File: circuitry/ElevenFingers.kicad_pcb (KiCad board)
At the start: 2 copper layers, 5.1 x 5.1 mm, 95 parts, among them J1 OLED, SW1 MX, SW10 MX, SW11 MX, SW12 MX, SW13 MX, SW14 MX, SW15 MX, SW16 MX, SW17 MX, SW18 MX, SW19 MX, SW2 MX, SW20 MX, SW21 MX, SW22 MX, SW23 MX, SW24 MX, SW25 MX, SW26 MX, SW27 MX, SW28 MX, SW29 MX, SW3 MX, SW30 MX, SW4 MX, SW5 MX, SW6 MX, SW7 MX, SW8 MX, SW9 MX, U1 ProMicro, U2 TRRS

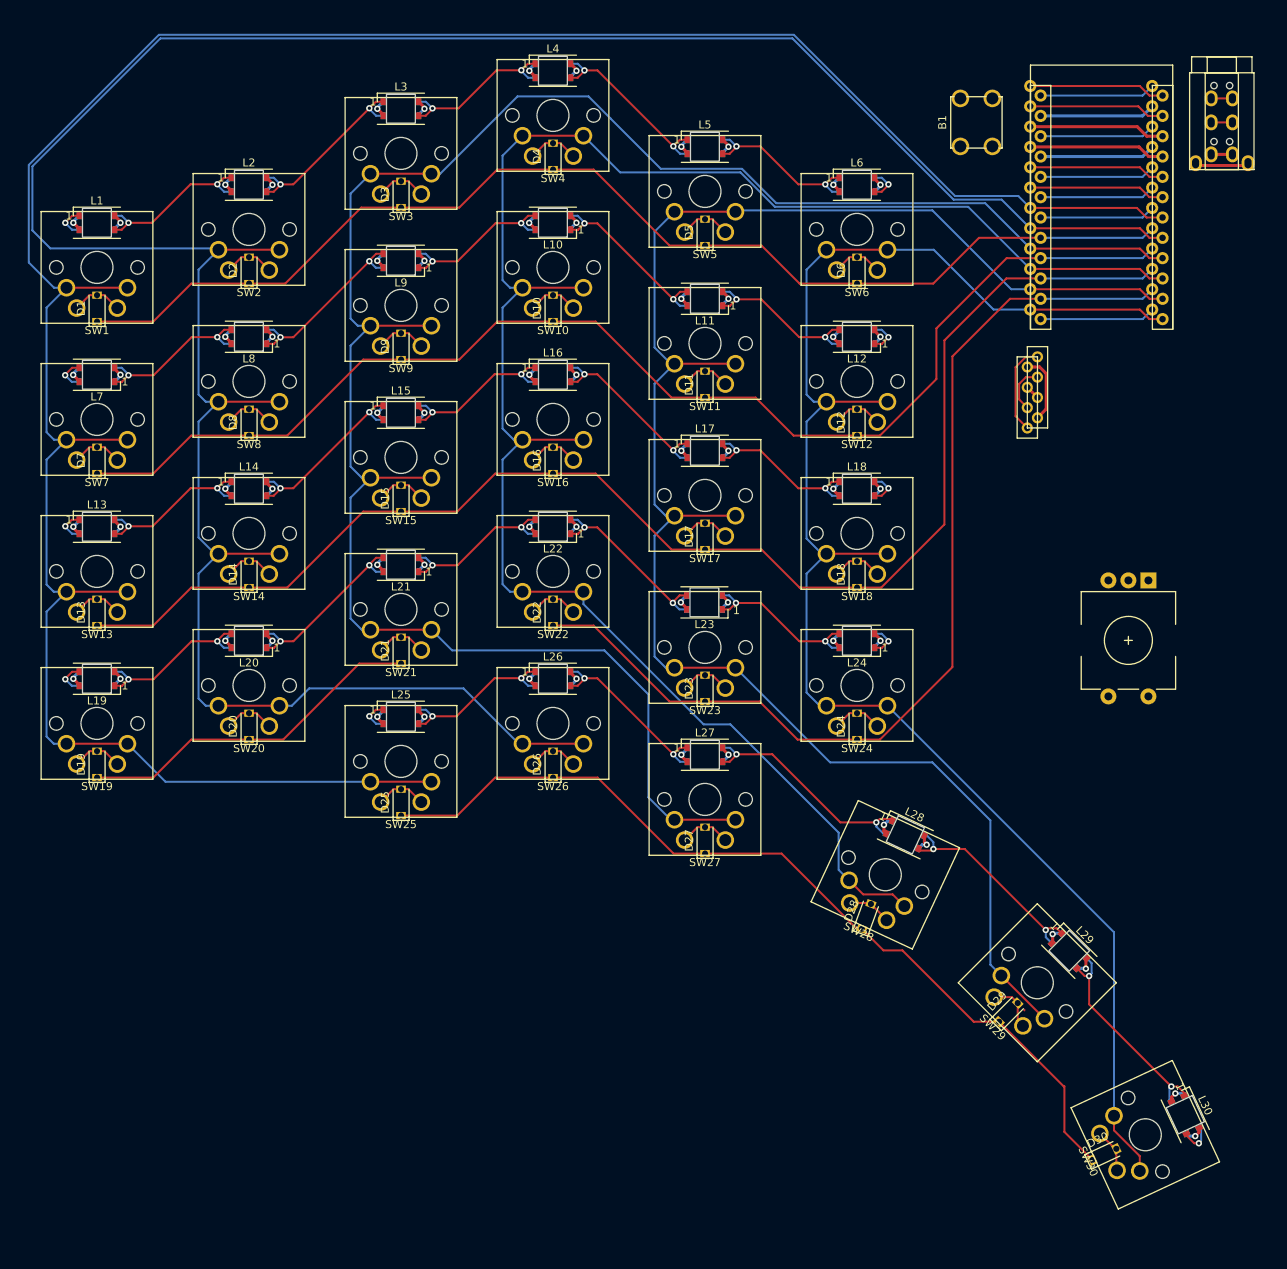
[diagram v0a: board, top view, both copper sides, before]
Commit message: pwr and gnd routed for leds, (not to promicro, and not across rows)
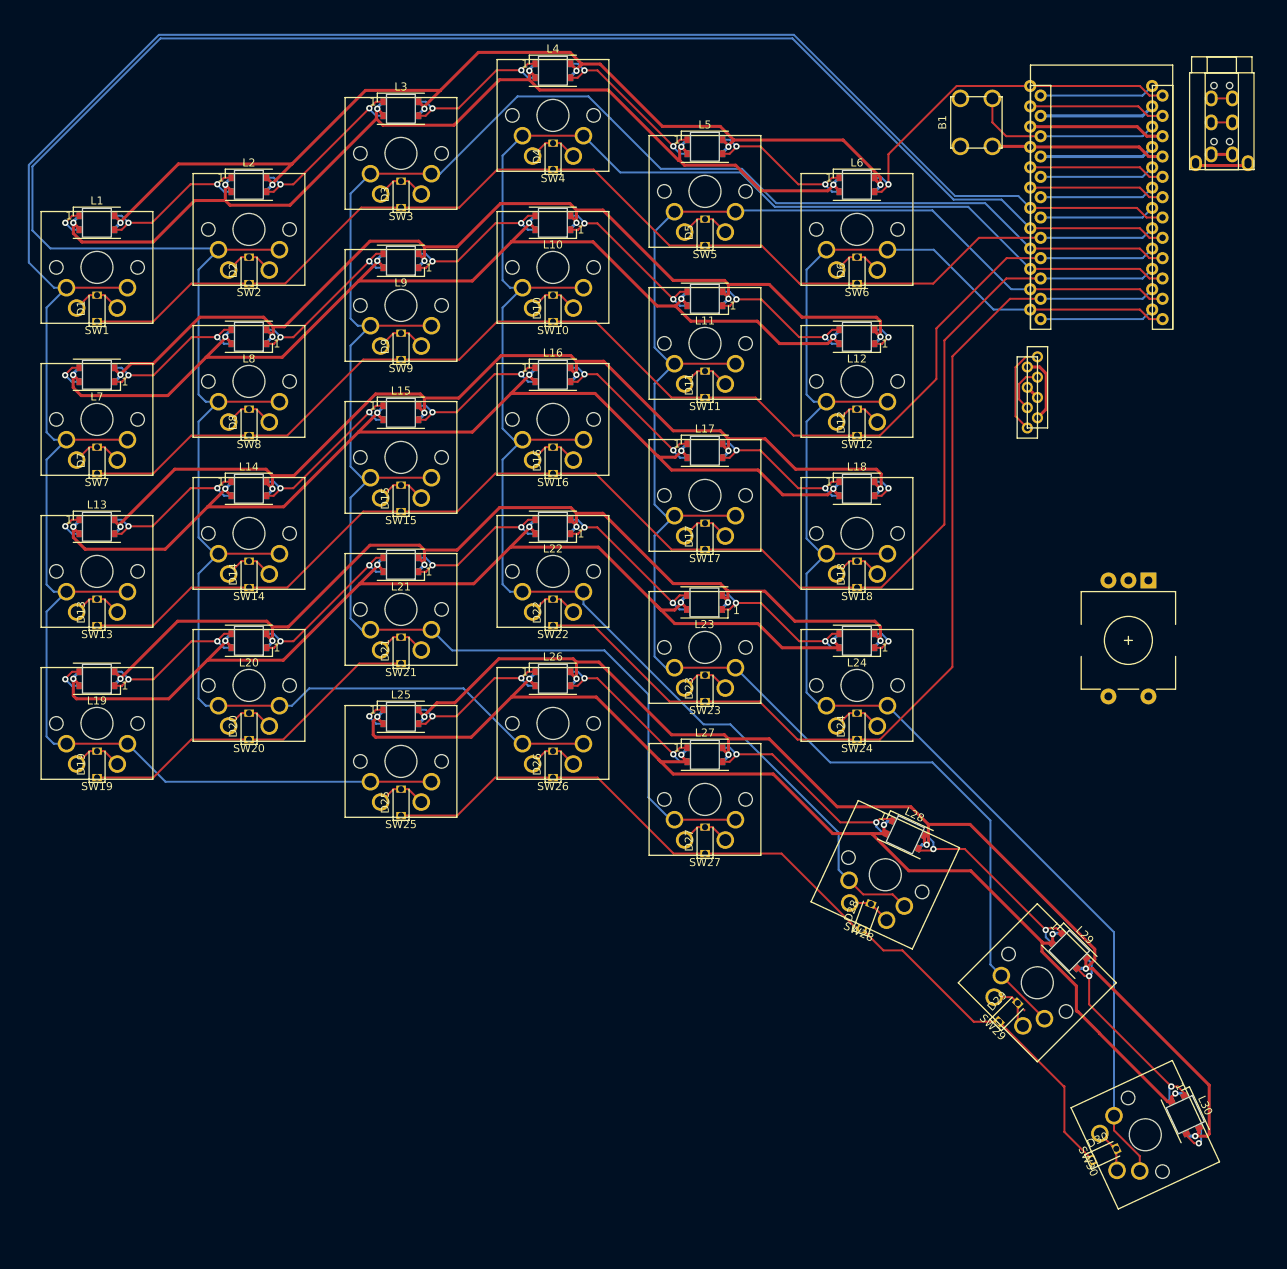
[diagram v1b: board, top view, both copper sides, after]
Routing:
- net GND: track 135.4 -> 767.9 mm
- net VCC: track 89.5 -> 708.5 mm
- net LED: track 21.2 -> 46.3 mm
- net Net-(B1-Pad1): track 14.4 -> 24.2 mm

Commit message: completed tracing?
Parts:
- moved J1 3.66 mm to (158.6, 88.4), turned to 0 degrees
- moved U2 1.29 mm to (176.4, 54.9)
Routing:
- net GND: track 767.9 -> 1000.0 mm
- net VCC: track 708.5 -> 921.5 mm
- net ENC_A: track 14.4 -> 68.4 mm
- net ENC_B: track 14.4 -> 66.5 mm
- net col1: track 328.1 -> 288.1 mm
- net Net-(J1-Pad1): track 28.5 -> 55.5 mm
- net Net-(J1-Pad2): track 23.1 -> 48.9 mm
- net col0: track 312.6 -> 293.8 mm
- net SERIAL: track 19.7 -> 24.8 mm
- net LED: track 46.3 -> 47.4 mm
- net Net-(B1-Pad1): track 24.2 -> 23.3 mm

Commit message: finished tracing and error checking
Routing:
- net row4: track 126.0 -> 267.9 mm
- net Net-(L24-Pad2): track 8.51 -> 109.3 mm
- net Net-(L13-Pad2): track 8.43 -> 29.9 mm
- net Net-(L1-Pad2): track 8.44 -> 29.8 mm
- net row3: track 170.8 -> 191.7 mm
- net Net-(L12-Pad2): track 8.44 -> 28.5 mm
- net col1: track 288.1 -> 276.6 mm
- net col0: track 293.8 -> 284.8 mm
- net GND: track 1000.0 -> 998.4 mm
- net col5: track 204.7 -> 203.2 mm
- net Net-(D29-Pad2): track 6.45 -> 5.45 mm
- net ENC_A: track 68.4 -> 67.4 mm
- net col4: track 220.6 -> 219.9 mm
- net col2: track 255.1 -> 254.6 mm

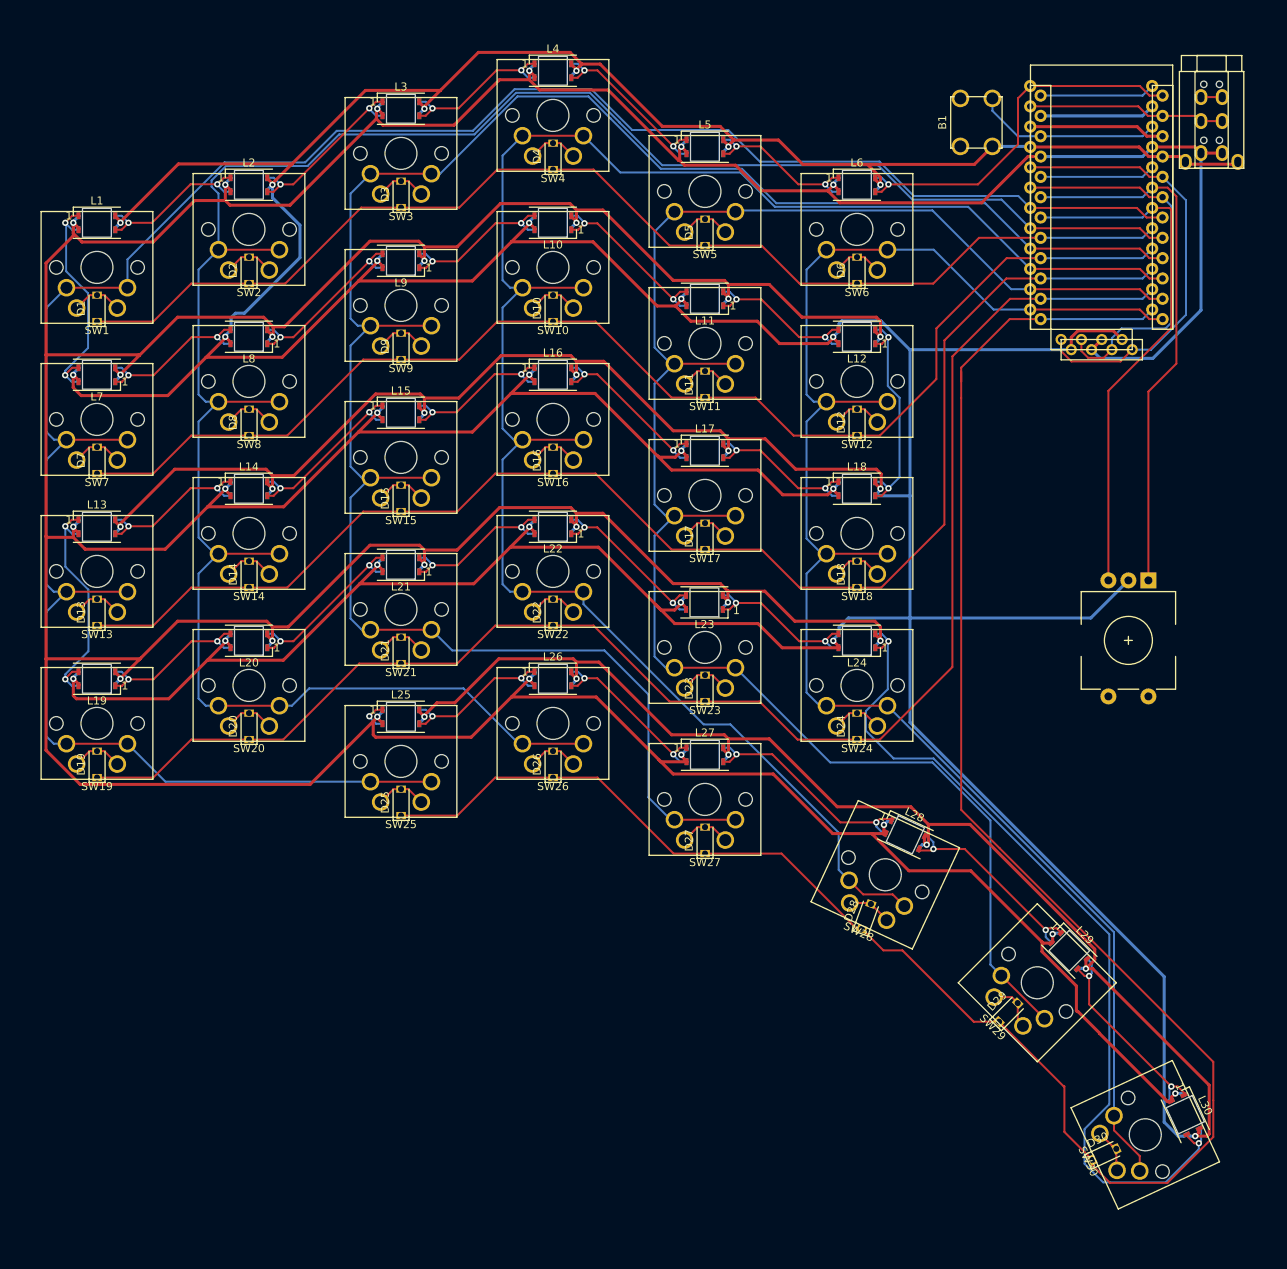
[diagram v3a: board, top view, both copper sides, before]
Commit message: tightened horizontal spacing of components
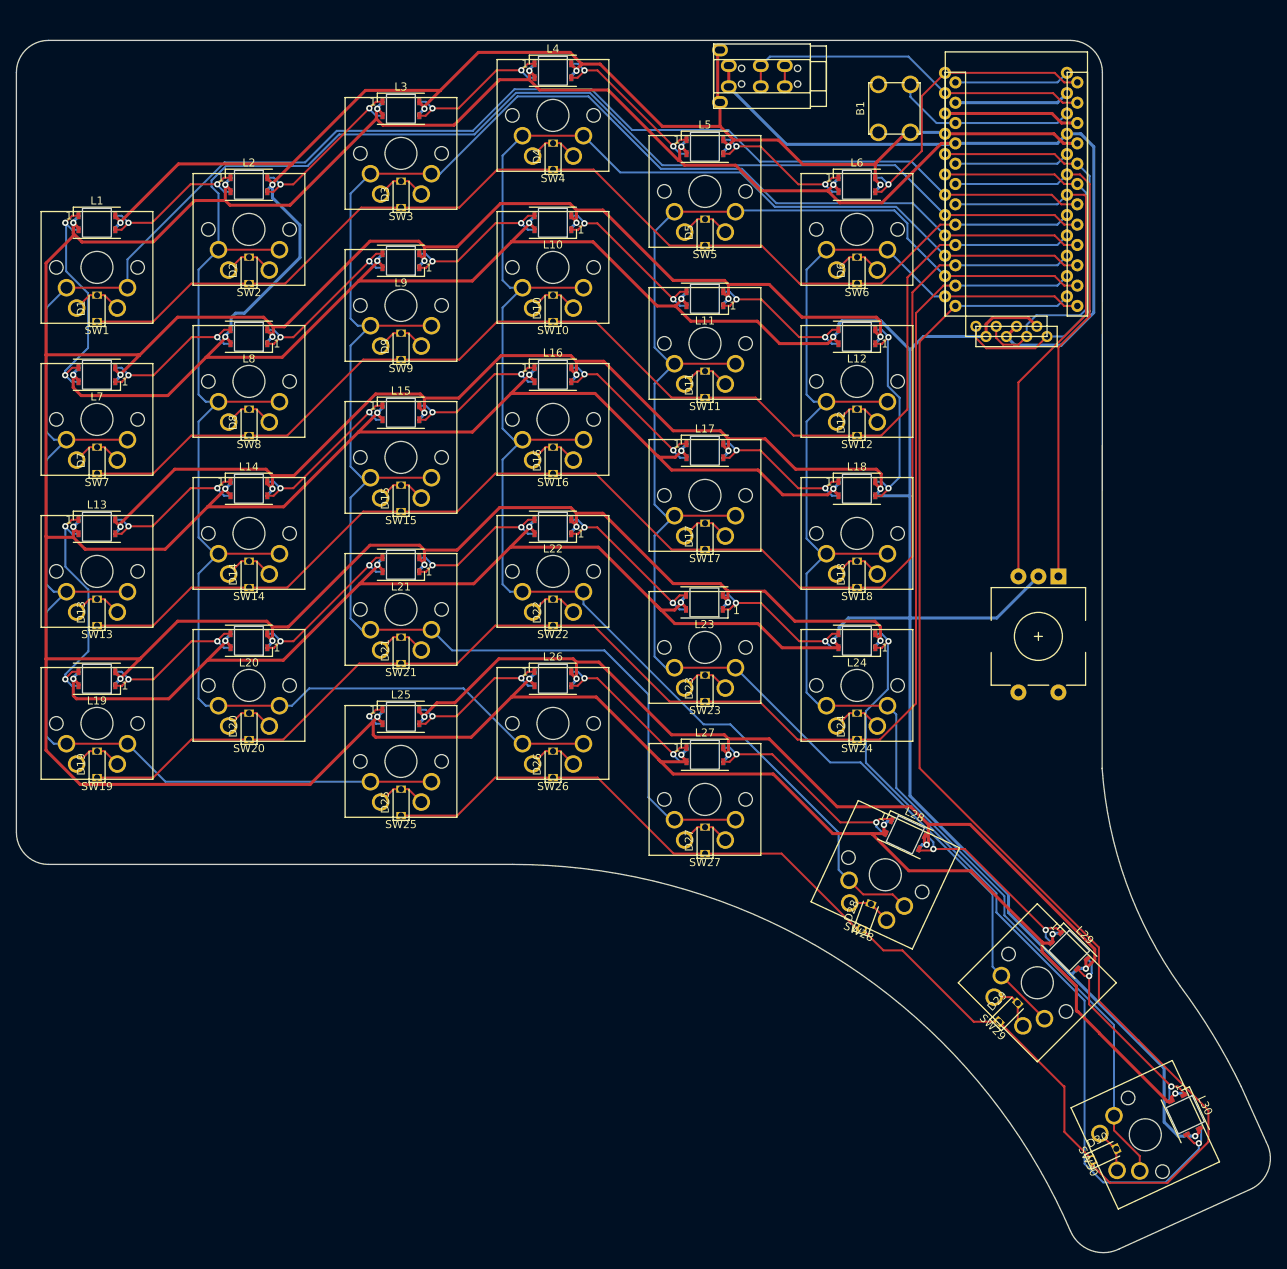
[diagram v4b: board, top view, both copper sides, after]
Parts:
- moved U2 49.2 mm to (127.2, 54.5), turned to -90 degrees
- moved E1 11.3 mm to (155.8, 125.5)
- moved U1 10.8 mm to (152.9, 69.8)
- moved J1 10.8 mm to (147.9, 86.7)
- moved B1 10.4 mm to (137.8, 59.5)
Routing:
- net GND: track 998.4 -> 938.1 mm
- net SERIAL: track 24.8 -> 45.1 mm
- net VCC: track 921.4 -> 937.8 mm
- net col4: track 219.9 -> 204.4 mm
- net col0: track 284.8 -> 273.4 mm
- net col5: track 203.2 -> 191.9 mm
- net col3: track 235.9 -> 224.6 mm
- net col1: track 276.6 -> 265.3 mm
- net col2: track 254.6 -> 243.2 mm
- net row0: track 148.5 -> 138.6 mm
- net LED: track 47.4 -> 38.1 mm
- net Net-(L24-Pad2): track 109.3 -> 103.8 mm
- net row3: track 191.7 -> 187.6 mm
- net row2: track 175.6 -> 171.5 mm
- net row1: track 159.1 -> 155.0 mm
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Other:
- board size 5.1 x 5.1 mm -> 156.7 x 151.5 mm

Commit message: completed plate layers and edge cuts
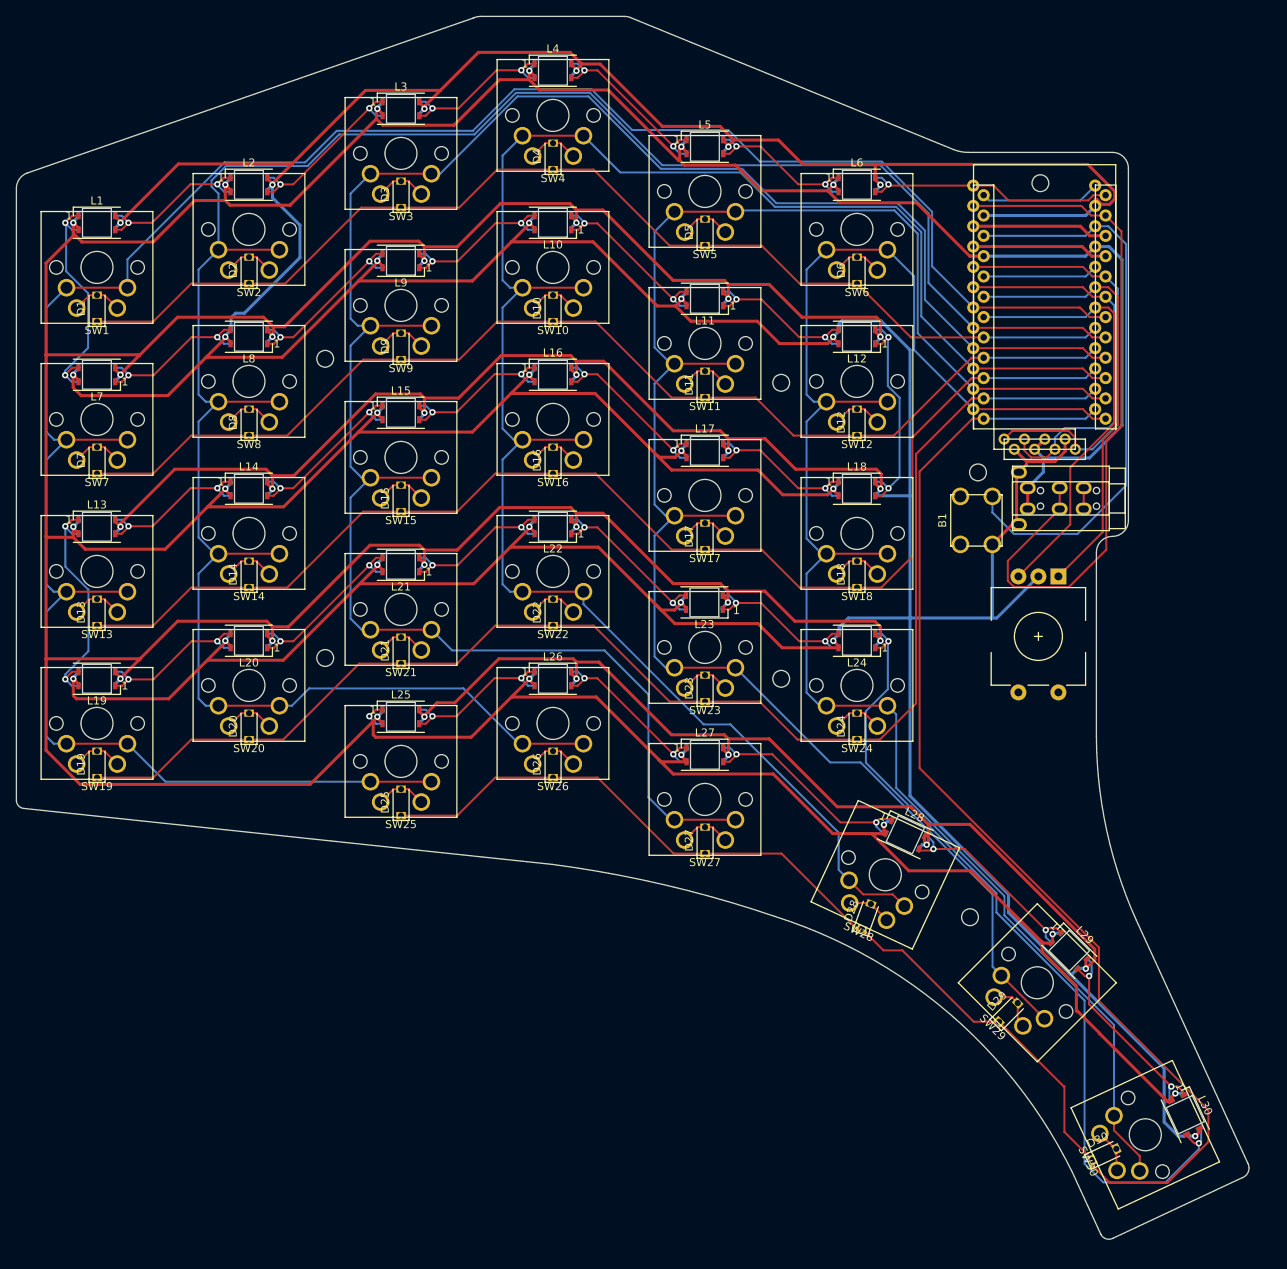
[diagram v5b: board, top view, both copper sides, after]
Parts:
- moved U2 64.7 mm to (164.6, 107.3)
- moved B1 52.5 mm to (148.0, 111.0)
- moved U1 14.5 mm to (156.4, 83.9)
- moved J1 14.5 mm to (151.5, 100.8)
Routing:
- net Net-(B1-Pad1): track 24.5 -> 71.7 mm
- net SERIAL: track 45.1 -> 89.3 mm
- net GND: track 938.1 -> 965.8 mm
- net VCC: track 937.8 -> 914.4 mm
- net col3: track 224.6 -> 240.2 mm
- net col4: track 204.4 -> 220.0 mm
- net col5: track 191.9 -> 206.6 mm
- net col1: track 265.3 -> 279.7 mm
- net col2: track 243.2 -> 257.7 mm
- net col0: track 273.4 -> 286.8 mm
- net ENC_B: track 67.9 -> 55.0 mm
- net row2: track 171.5 -> 158.6 mm
- net ENC_A: track 68.4 -> 55.8 mm
- net row3: track 187.6 -> 175.0 mm
- net row1: track 155.0 -> 143.1 mm
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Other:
- board size 156.7 x 151.5 mm -> 154.1 x 152.9 mm
